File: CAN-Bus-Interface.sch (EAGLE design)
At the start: 18 parts, among them J1 M13, J4 MST4V, U1 MCP2515-P, U2 MCP2551-P

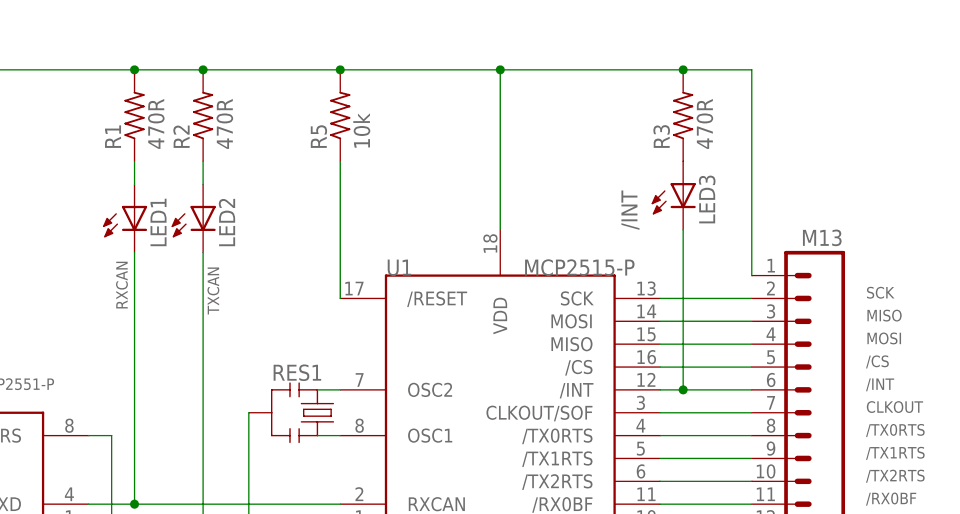
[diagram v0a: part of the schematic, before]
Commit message: added values for connectors
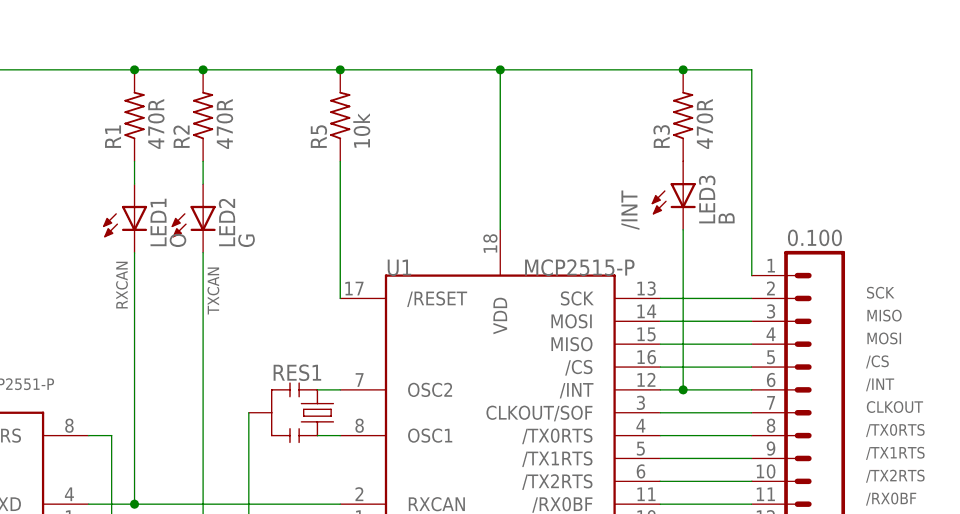
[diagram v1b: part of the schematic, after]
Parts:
- J1: value M13 -> 0.100
- LED1: value (none) -> O
- LED2: value (none) -> G
- LED3: value (none) -> B
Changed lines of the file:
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@@
 <part name="U1" library="MCP" deviceset="MCP2515" device="-P"/>
 <part name="L1" library="MCP" deviceset="ZJYS51R5" device="-2P"/>
-<part name="LED1" library="MCP" deviceset="LED" device="B155"/>
-<part name="LED2" library="MCP" deviceset="LED" device="B155"/>
-<part name="LED3" library="MCP" deviceset="LED" device="B155"/>
+<part name="LED1" library="MCP" deviceset="LED" device="B155" value="O"/>
+<part name="LED2" library="MCP" deviceset="LED" device="B155" value="G"/>
+<part name="LED3" library="MCP" deviceset="LED" device="B155" value="B"/>
 <part name="C2" library="SparkFun" deviceset="CAP" device="PTH2" value="0.1uf"/>
 <part name="C1" library="SparkFun" deviceset="CAP" device="PTH2" value="0.1uf"/>
 <part name="P+7" library="supply1" deviceset="VCC" device=""/>
 <part name="V12" library="supply2" deviceset="GND" device=""/>
-<part name="J1" library="SparkFun" deviceset="M13" device=""/>
+<part name="J1" library="SparkFun" deviceset="M13" device="" value="0.100"/>
 <part name="P+1" library="supply1" deviceset="VCC" device=""/>
 <part name="CANPWR" library="pinhead" deviceset="PINHD-1X2" device=""/>

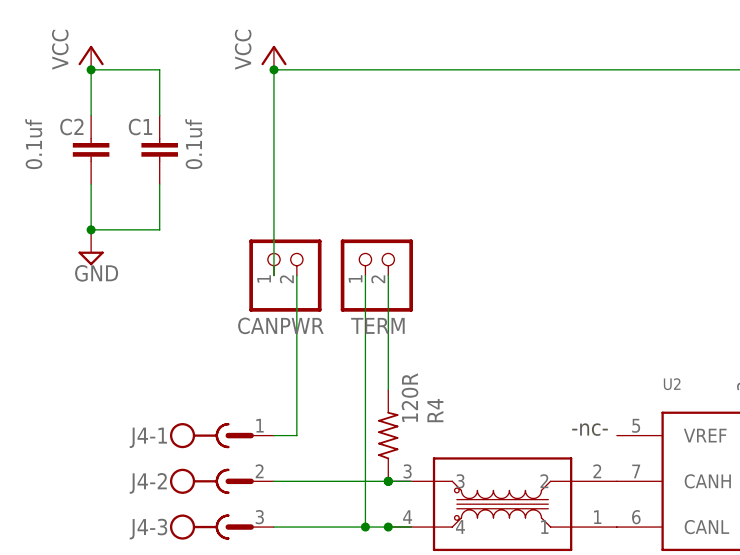
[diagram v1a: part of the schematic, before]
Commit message: added values for connectors
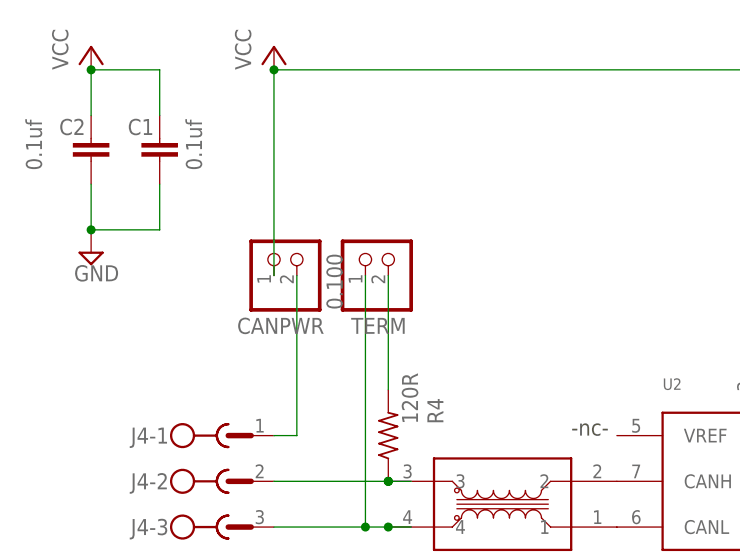
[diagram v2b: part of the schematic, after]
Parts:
- CANPWR: value (none) -> 0.100
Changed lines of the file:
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@@
 <part name="J1" library="SparkFun" deviceset="M13" device="" value="0.100"/>
 <part name="P+1" library="supply1" deviceset="VCC" device=""/>
-<part name="CANPWR" library="pinhead" deviceset="PINHD-1X2" device=""/>
+<part name="CANPWR" library="pinhead" deviceset="PINHD-1X2" device="" value="0.100"/>
 </parts>
 <sheets>

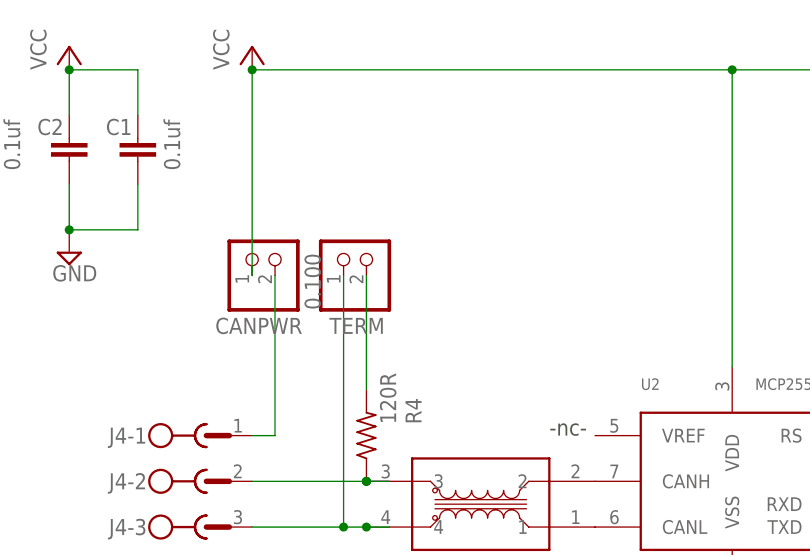
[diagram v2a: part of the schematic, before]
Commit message: added values for connectors
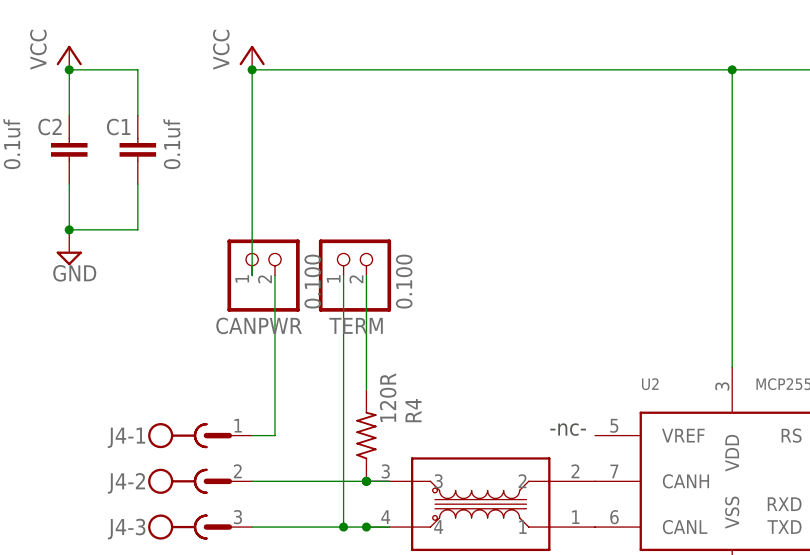
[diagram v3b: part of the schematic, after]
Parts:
- TERM: value (none) -> 0.100
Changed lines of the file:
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@@
 <part name="R4" library="rcl" deviceset="R-US_" device="0204/5" value="120R"/>
 <part name="U2" library="MCP" deviceset="MCP2551" device="-P"/>
-<part name="TERM" library="pinhead" deviceset="PINHD-1X2" device=""/>
+<part name="TERM" library="pinhead" deviceset="PINHD-1X2" device="" value="0.100"/>
 <part name="J4" library="con-phoenix-508" deviceset="MST4V" device=""/>
 <part name="V6" library="supply2" deviceset="GND" device=""/>

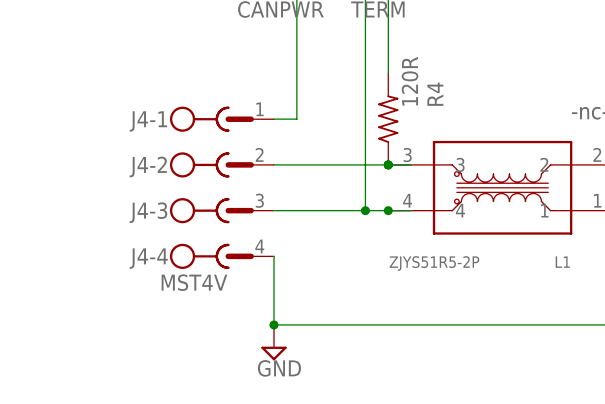
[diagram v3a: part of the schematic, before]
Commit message: normalized values
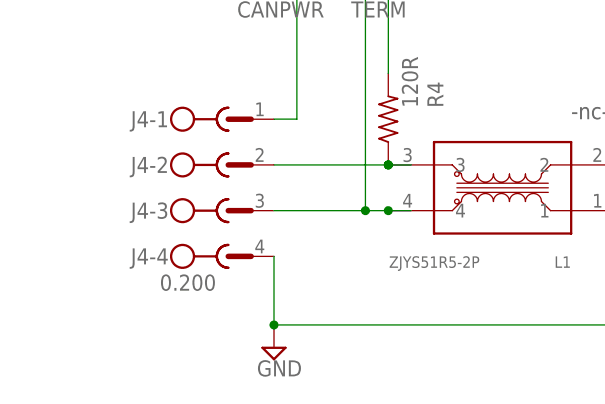
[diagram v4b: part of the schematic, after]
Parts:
- J4: value MST4V -> 0.200
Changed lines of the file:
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@@
 <part name="U2" library="MCP" deviceset="MCP2551" device="-P"/>
 <part name="TERM" library="pinhead" deviceset="PINHD-1X2" device="" value="0.100"/>
-<part name="J4" library="con-phoenix-508" deviceset="MST4V" device=""/>
+<part name="J4" library="con-phoenix-508" deviceset="MST4V" device="" value="0.200"/>
 <part name="V6" library="supply2" deviceset="GND" device=""/>
 <part name="R1" library="rcl" deviceset="R-US_" device="0204/5" value="470R"/>
